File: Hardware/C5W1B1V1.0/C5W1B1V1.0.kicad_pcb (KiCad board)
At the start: 4 copper layers, 100 x 100 mm, 108 parts, among them IC1 ESP32-C3-WROOM-02-N4, IC2 USBLC6-2P6, J1 Conn_02x20_Counter_Clockwise, J2 Conn_02x20_Counter_Clockwise, J3 Conn_01x13_Male, J4 Conn_01x04, J5 USB4105GFA120, SW1 SW_Push_Dual, SW2 SW_Push_Dual, SW3 SW_Push_Dual, SW4 SW_Push_Dual, U1 STM32H735IGT6, U2 MB85RS512TPNF-G-JNERE1, U3 W25N512GVEIG, U4 APS6404L-3SQR-SN, U5 LSM303AHTR, U6 VL53L0CXV0DH_1, U7 BME688, U8 ISM330ISN, U9 LD1117S33TR_SOT223, Y1 ECS-250-8-36CKM-TR3, Y2 830106545501, Y3 830106545501

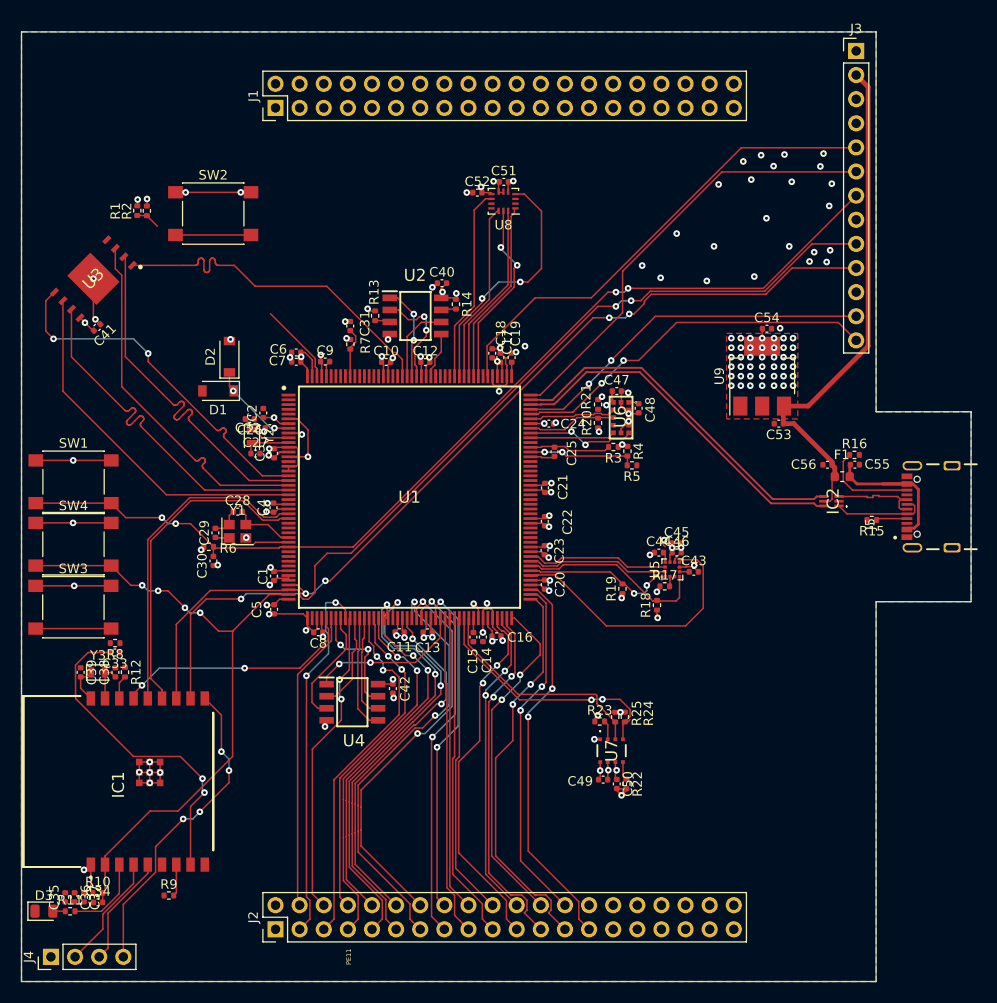
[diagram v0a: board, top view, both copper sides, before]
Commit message: Linie PC0-PE13
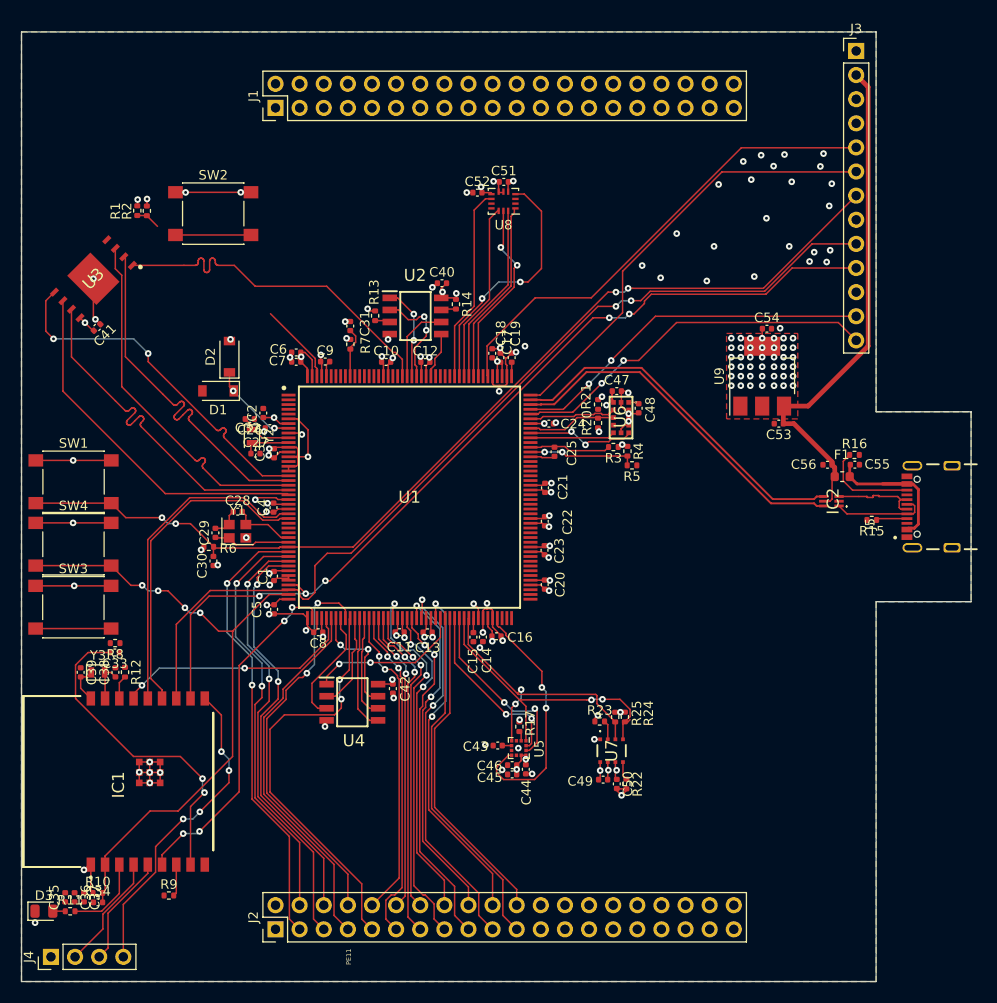
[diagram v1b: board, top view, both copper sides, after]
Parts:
- removed R18, R19: 10k/5%/0.063W, Resistor_SMD:R_0402_1005Metric
- moved C45 29.9 mm to (91.7, 118.2), turned to 180 degrees
- moved C46 28.3 mm to (91.7, 117.2), turned to 180 degrees
- moved C43 27.6 mm to (90.2, 115.2), turned to 180 degrees
- moved C44 26.8 mm to (93.1, 117.7), turned to 90 degrees
- moved U5 24.8 mm to (92.4, 115.4), turned to 270 degrees
- moved R17 21.3 mm to (92.4, 113.2), turned to 270 degrees
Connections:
- J2 pad 10: PF14 -> PF11
- J2 pad 11: PG0 -> PF12
- J2 pad 12: PG1 -> PF13
- J2 pad 13: PE7 -> PF14
- J2 pad 14: PE8 -> PF15
- J2 pad 15: PE9 -> PG0
- J2 pad 16: PE10 -> PG1
- J2 pad 17: PE12 -> PE7
- J2 pad 18: PE13 -> PE8
- J2 pad 19: PE14 -> PE9
- J2 pad 20: PE15 -> PE10
- J2 pad 21: PB12 -> PE12
- J2 pad 22: PB13 -> PE13
- J2 pad 23: PB14 -> Net-(J2-Pad23)
- J2 pad 24: PB15 -> Net-(J2-Pad24)
- J2 pad 25: PD8 -> Net-(J2-Pad25)
- J2 pad 26: PD9 -> Net-(J2-Pad26)
- J2 pad 27: PD10 -> Net-(J2-Pad27)
- J2 pad 3: PC4 -> PC0
- J2 pad 4: PA5 -> PC1
- J2 pad 5: PF11 -> PC2
- J2 pad 6: PC5 -> PC3
- J2 pad 7: PF13 -> PA5
- J2 pad 8: PF12 -> PC4
- J2 pad 9: PF15 -> PC5
- U1 pad 76: PE14 -> LSM303_INT1
- U1 pad 77: PE15 -> LSM303_INT2
- U1 pad 85: PB12 -> LSM303_INT_MAG
- U1 pad 94: LSM303_INT_MAG -> Net-(U1-Pad94)
- U1 pad 95: LSM303_SCL -> Net-(U1-Pad95)
- U1 pad 96: LSM303_SDA -> Net-(U1-Pad96)
- U1 pad 97: LSM303_INT1 -> Net-(U1-Pad97)
- U1 pad 98: LSM303_INT2 -> Net-(U1-Pad98)
- U5 pad 1: LSM303_SCL -> BME688_SCL
- U5 pad 4: LSM303_SDA -> BME688_SDA
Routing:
- net PC0: track 0.00 -> 47.4 mm, vias 0 -> 2
- net PC2: track 0.00 -> 46.1 mm, vias 0 -> 2
- net PC1: track 0.00 -> 44.0 mm, vias 0 -> 2
- net PC3: track 0.00 -> 43.0 mm, vias 0 -> 2
- net PD8: track 41.7 -> 0.00 mm, vias 2 -> 0
- net PD10: track 40.8 -> 0.00 mm, vias 2 -> 0
- net PB12: track 38.1 -> 0.00 mm, vias 2 -> 0
- net PB14: track 37.5 -> 0.00 mm, vias 2 -> 0
- net PD9: track 36.9 -> 0.00 mm, vias 2 -> 0
- net STM_ESP_PIN1: track 0.00 -> 36.8 mm, vias 0 -> 4
- net PB15: track 35.9 -> 0.00 mm, vias 2 -> 0
- net PE14: track 34.6 -> 0.00 mm
- net PB13: track 33.1 -> 0.00 mm, vias 2 -> 0
- net PE15: track 32.0 -> 0.00 mm
- net LSM303_SDA: track 19.9 -> 0.00 mm
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
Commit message: Rozlana masa
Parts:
- added C57: 100n/16V/X5R, Capacitor_SMD:C_0402_1005Metric, F.Cu at (99.8, 86.8)
- added C58: 100n/16V/X5R, Capacitor_SMD:C_0402_1005Metric, F.Cu at (99.8, 87.8)
- added C59: 100n/16V/X5R, Capacitor_SMD:C_0402_1005Metric, F.Cu at (125.6, 108.6)
- added C60: 100n/16V/X5R, Capacitor_SMD:C_0402_1005Metric, F.Cu at (45.9, 59.1)
- added C61: 10u/16V/X5R, Capacitor_SMD:C_0603_1608Metric, F.Cu at (54.5, 50.2)
- added C63: 185p/16V/C0G, Capacitor_SMD:C_0402_1005Metric, F.Cu at (61.1, 49.5)
- added C66: 10u/25V/X5R, Capacitor_SMD:C_1206_3216Metric, F.Cu at (62.9, 51.0)
- added C67: 10u/25V/X5R, Capacitor_SMD:C_1206_3216Metric, F.Cu at (61.0, 54.5)
- added D4: LED, LED_SMD:LED_0805_2012Metric, F.Cu at (127.5, 112.4)
- added D5: LED, LED_SMD:LED_0805_2012Metric, F.Cu at (127.5, 114.5)
- added D6: WS2812B, LED_SMD:LED_WS2812B_PLCC4_5.0x5.0mm_P3.2mm, F.Cu at (126.6, 104.7)
- added D7: BZX384B3V3-E3-08, Diode_SMD:D_SOD-323, F.Cu at (54.4, 55.5)
- added D8: PMEG4010CEGWX, Diode_SMD:D_SOD-123, F.Cu at (60.8, 47.4)
- added F3: SF-0603FP015F-2, Fuse:Fuse_0603_1608Metric, F.Cu at (63.5, 56.5)
- added J6: Conn_01x08_Male, Connector_PinHeader_2.54mm:PinHeader_1x08_P2.54mm_Vertical, F.Cu at (43.5, 42.3)
- added J7: Conn_01x02_Male, Connector_PinHeader_2.54mm:PinHeader_1x02_P2.54mm_Vertical, F.Cu at (41.9, 74.5)
- added L2: SRN6045TA-101M, Footprints:SRN6045TA220M, F.Cu at (54.0, 44.6)
- added R18: 10k/5%/0.063W, Resistor_SMD:R_0402_1005Metric, F.Cu at (122.1, 119.3)
- added R19: 10k/5%/0.063W, Resistor_SMD:R_0402_1005Metric, F.Cu at (122.1, 129.6)
- added R26: 470/5%/0.063W, Resistor_SMD:R_0402_1005Metric, F.Cu at (122.7, 101.9)
- added R27: 470/5%/0.063W, Resistor_SMD:R_0402_1005Metric, F.Cu at (124.5, 112.3)
- added R28: 470/5%/0.063W, Resistor_SMD:R_0402_1005Metric, F.Cu at (124.6, 114.5)
- added R29: 10K/5%/0.063W, Resistor_SMD:R_0402_1005Metric, F.Cu at (56.6, 52.8)
- added R30: 10K/5%/0.063W, Resistor_SMD:R_0402_1005Metric, F.Cu at (56.3, 56.7)
- added R31: 85.6K/5%/0.063W, Resistor_SMD:R_0402_1005Metric, F.Cu at (60.1, 49.6)
- added R32: 10K/5%/0.063W, Resistor_SMD:R_0402_1005Metric, F.Cu at (60.1, 51.5)
- added R33: 3.3K/5%/0.063W, Resistor_SMD:R_0402_1005Metric, F.Cu at (56.3, 55.7)
- added SW5: SW_Push_Dual, Button_Switch_SMD:SW_Push_1P1T_NO_6x6mm_H9.5mm, F.Cu at (125.9, 123.8)
- added SW6: SW_Push_Dual, Button_Switch_SMD:SW_Push_1P1T_NO_6x6mm_H9.5mm, F.Cu at (125.9, 134.1)
- added U11: LMR62421XSD_NOPB, Footprints:SON95P300X300X80-7N, F.Cu at (57.4, 50.5)
- moved R1 2.11 mm to (51.3, 60.7)
- moved R2 2.11 mm to (52.3, 60.8)
- moved SW2 2.11 mm to (59.3, 61.0)
- moved C18 0.14 mm to (90.6, 74.3)
- moved C20 0.13 mm to (95.1, 98.1)
- moved C51 0.09 mm to (90.8, 55.7)
- moved C52 0.08 mm to (87.9, 56.9)
- renumbered IC2 to U10, IC1 to U12
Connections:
- J1 pad 1: Net-(J1-Pad1) -> +12V
- J1 pad 10: Net-(J1-Pad10) -> PE0
- J1 pad 11: Net-(J1-Pad11) -> PB9
- J1 pad 12: Net-(J1-Pad12) -> PB8
- J1 pad 13: Net-(J1-Pad13) -> PB7
- J1 pad 14: Net-(J1-Pad14) -> PB6
- J1 pad 15: Net-(J1-Pad15) -> PB5
- J1 pad 16: Net-(J1-Pad16) -> PB4
- J1 pad 17: Net-(J1-Pad17) -> PB3
- J1 pad 18: Net-(J1-Pad18) -> PG15
- J1 pad 19: Net-(J1-Pad19) -> PG14
- J1 pad 2: Net-(J1-Pad2) -> +12V
- J1 pad 20: Net-(J1-Pad20) -> PG13
- J1 pad 21: Net-(J1-Pad21) -> PD6
- J1 pad 22: Net-(J1-Pad22) -> PD5
- J1 pad 23: Net-(J1-Pad23) -> PD3
- J1 pad 24: Net-(J1-Pad24) -> PD4
- J1 pad 25: Net-(J1-Pad25) -> PA15
- J1 pad 26: Net-(J1-Pad26) -> PG4
- J1 pad 27: Net-(J1-Pad27) -> PK0
- J1 pad 28: Net-(J1-Pad28) -> PK1
- J1 pad 29: Net-(J1-Pad29) -> PK2
- J1 pad 3: Net-(J1-Pad3) -> GND
- J1 pad 30: Net-(J1-Pad30) -> PG2
- J1 pad 31: Net-(J1-Pad31) -> PG3
- J1 pad 32: Net-(J1-Pad32) -> +5V
- J1 pad 33: Net-(J1-Pad33) -> +3V3
- J1 pad 34: Net-(J1-Pad34) -> +5V
- J1 pad 35: Net-(J1-Pad35) -> +3V3
- J1 pad 36: Net-(J1-Pad36) -> +3V3
- J1 pad 37: Net-(J1-Pad37) -> GND
- J1 pad 38: Net-(J1-Pad38) -> GND
- J1 pad 39: Net-(J1-Pad39) -> GND
- J1 pad 4: Net-(J1-Pad4) -> GND
- J1 pad 40: Net-(J1-Pad40) -> GND
- J1 pad 5: Net-(J1-Pad5) -> PF5
- J1 pad 6: Net-(J1-Pad6) -> PF8
- J1 pad 7: Net-(J1-Pad7) -> PF9
- J1 pad 8: Net-(J1-Pad8) -> PF10
- J1 pad 9: Net-(J1-Pad9) -> PE1
- J2 pad 1: Net-(J2-Pad1) -> GND
- J2 pad 2: Net-(J2-Pad2) -> GND
- J2 pad 23: Net-(J2-Pad23) -> PB13
- J2 pad 24: Net-(J2-Pad24) -> PB14
- J2 pad 25: Net-(J2-Pad25) -> PB15
- J2 pad 26: Net-(J2-Pad26) -> PD8
- J2 pad 27: Net-(J2-Pad27) -> PD9
- J2 pad 28: Net-(J2-Pad28) -> PD10
- J2 pad 29: Net-(J2-Pad29) -> PD11
- J2 pad 3: PC0 -> +3V3
- J2 pad 30: Net-(J2-Pad30) -> PD12
- J2 pad 31: Net-(J2-Pad31) -> PD13
- J2 pad 32: Net-(J2-Pad32) -> PD14
- J2 pad 33: Net-(J2-Pad33) -> PD15
- J2 pad 34: Net-(J2-Pad34) -> PJ8
- J2 pad 35: Net-(J2-Pad35) -> PJ9
- J2 pad 36: Net-(J2-Pad36) -> PJ10
- J2 pad 37: Net-(J2-Pad37) -> PJ11
- J2 pad 38: Net-(J2-Pad38) -> +5V
- J2 pad 39: Net-(J2-Pad39) -> +3V3
- J2 pad 4: PC1 -> +3V3
- J2 pad 40: Net-(J2-Pad40) -> GND
- U1 pad 115: PG5 -> BUTTON2
- U1 pad 116: PG6 -> BUTTON1
- U1 pad 117: PG7 -> LED2
- U1 pad 118: PG8 -> LED1
- U1 pad 122: PC6 -> WS2812
- U1 pad 2: SSD1331_DC -> SSD1331_RES
- U1 pad 3: SSD1331_RES -> SSD1331_DC
- U1 pad 34: PC0 -> 12V_DC_V
- U1 pad 35: PC1 -> 12V_EN
- U1 pad 94: Net-(U1-Pad94) -> PD11
- U1 pad 95: Net-(U1-Pad95) -> PD12
- U1 pad 96: Net-(U1-Pad96) -> PD13
- U1 pad 97: Net-(U1-Pad97) -> PD14
- U1 pad 98: Net-(U1-Pad98) -> PD15
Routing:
- net +5V: track 54.3 -> 232.8 mm, vias 0 -> 4
- net 12V_EN: track 0.00 -> 72.2 mm, vias 0 -> 2
- net BUTTON2: track 0.00 -> 69.2 mm, vias 0 -> 2
- net 12V_DC_V: track 0.00 -> 67.8 mm, vias 0 -> 2
- net BUTTON1: track 0.00 -> 59.9 mm, vias 0 -> 2
- net PF10: track 0.00 -> 58.5 mm, vias 0 -> 2
- net PG2: track 0.00 -> 57.2 mm, vias 0 -> 4
- net PF8: track 0.00 -> 55.8 mm, vias 0 -> 2
- net PJ11: track 0.00 -> 54.3 mm, vias 0 -> 2
- net PF9: track 0.00 -> 53.9 mm, vias 0 -> 2
- net PG3: track 0.00 -> 53.9 mm, vias 0 -> 5
- net PK1: track 0.00 -> 53.2 mm, vias 0 -> 4
- net PD15: track 0.00 -> 51.5 mm, vias 0 -> 2
- net PK0: track 0.00 -> 50.4 mm, vias 0 -> 4
- net SSD1331_CS: track 1.46 -> 51.7 mm, vias 1 -> 4
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- added copper zone on B.Cu, net +3V3
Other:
- board text added: "12V"
- board text added: "3V3"
- board text added: "5V"
- board text added: "ESP_GPIO10"
- board text added: "ESP_GPIO5"
- board text added: "ESP_GPIO6"
- board text added: "ESP_RX"
- board text added: "ESP_TX"
- board text added: "GND"
- board text added: "PA15"
- board text added: "PA5"
- board text added: "PB13"
- board text added: "PB14"
- board text added: "PB15"
- board text added: "PB3"
- board text added: "PB4"
- board text added: "PB5"
- board text added: "PB6"
- board text added: "PB7"
- board text added: "PB8"
- board text added: "PB9"
- board text added: "PC2"
- board text added: "PC3"
- board text added: "PC4"
- board text added: "PC5"
- board text added: "PD10"
- board text added: "PD11"
- board text added: "PD12"
- board text added: "PD13"
- board text added: "PD14"
- board text added: "PD15"
- board text added: "PD3"
- board text added: "PD4"
- board text added: "PD5"
- board text added: "PD6"
- board text added: "PD8"
- board text added: "PD9"
- board text added: "PE0"
- board text added: "PE1"
- board text added: "PE10"
- board text added: "PE12"
- board text added: "PE13"
- board text added: "PE7"
- board text added: "PE8"
- board text added: "PE9"
- board text added: "PF10"
- board text added: "PF11"
- board text added: "PF12"
- board text added: "PF13"
- board text added: "PF14"
- board text added: "PF15"
- board text added: "PF5"
- board text added: "PF8"
- board text added: "PF9"
- board text added: "PG0"
- board text added: "PG1"
- board text added: "PG13"
- board text added: "PG14"
- board text added: "PG15"
- board text added: "PG2"
- board text added: "PG3"
- board text added: "PG4"
- board text added: "PJ10"
- board text added: "PJ11"
- board text added: "PJ8"
- board text added: "PJ9"
- board text added: "PK0"
- board text added: "PK1"
- board text added: "PK2"
- board text added: "STM_RST"
- board text added: "STM_RX"
- board text added: "STM_TX"
- board text added: "SWCLK"
- board text added: "SWDIO"
- board text removed: "PE11"

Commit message: Dodano opisy
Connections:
- U12 pad 15: STM_ESP_PIN2 -> Net-(U12-Pad15)
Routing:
- net GND: track 158.0 -> 159.7 mm, vias 686 -> 780
- net PD9: track 43.3 -> 44.6 mm
- net BME688_SDA: track 30.4 -> 29.5 mm
- net +3V3: track 117.7 -> 116.9 mm, vias 100 -> 99
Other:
- board text added: "A project done after a few beers, so I am not responsible for damages or mistakes :)"
- board text added: "All content included in the project (C5) can be copied without restriction"
- board text added: "C5W1B1V1.0"
- board text added: "I believe that knowledge should be shared, so this project is exempt from the copyright clause :)"
- board text added: "If it becomes a company I will let you know at https://github.com/MarcinWojewodzic"
- board text added: "If you are reading this, it means you can use all the resources Puszek's Incorporated As long as it does not become a company :)"
- board text added: "PG11"
- board text added: "PH3"
- board text added: "Puszek's incorporated"
- board text added: "Special greetings to my team in the company "Lars" (what are with me 30.06.2024) and my friend Igor, Who can use my work without restrictions Greetings, Marcin Wojewodzic"
- board text added: "The project has an educational purpose in the field: AI in embedded systems, WiFi connectivity in embedded systems"
- board text added: "https://github.com/MarcinWojewodzic/C5.git"

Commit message: End PCB
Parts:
- removed L2: SRN6045TA-101M, Footprints:SRN6045TA220M
- added L1: CBC3225T470MR, Inductor_SMD:L_1210_3225Metric, F.Cu at (56.1, 47.0)
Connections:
- U12 pad 15: Net-(U12-Pad15) -> STM_ESP_PIN2
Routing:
- net SWDIO: track 45.1 -> 50.7 mm
- net +5V: track 232.8 -> 229.0 mm
- net Net-(D8-Pad2): track 6.44 -> 4.05 mm
- net PB6: track 36.8 -> 35.9 mm
- net Net-(C63-Pad1): track 4.69 -> 5.54 mm
- net PB7: track 33.3 -> 32.6 mm
- net GND: vias 780 -> 786
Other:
- board text added: "https://github.com/MarcinWojewodzic"
- board text removed: "If it becomes a company I will let you know at https://github.com/MarcinWojewodzic"
- board text removed: "If you are reading this, it means you can use all the resources Puszek's Incorporated As long as it does not become a company :)"
- board text removed: "Special greetings to my team in the company "Lars" (what are with me 30.06.2024) and my friend Igor, Who can use my work without restrictions Greetings, Marcin Wojewodzic"
